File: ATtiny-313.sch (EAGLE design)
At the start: 17 parts, among them IC1 REG1117, IC2 ATtiny85

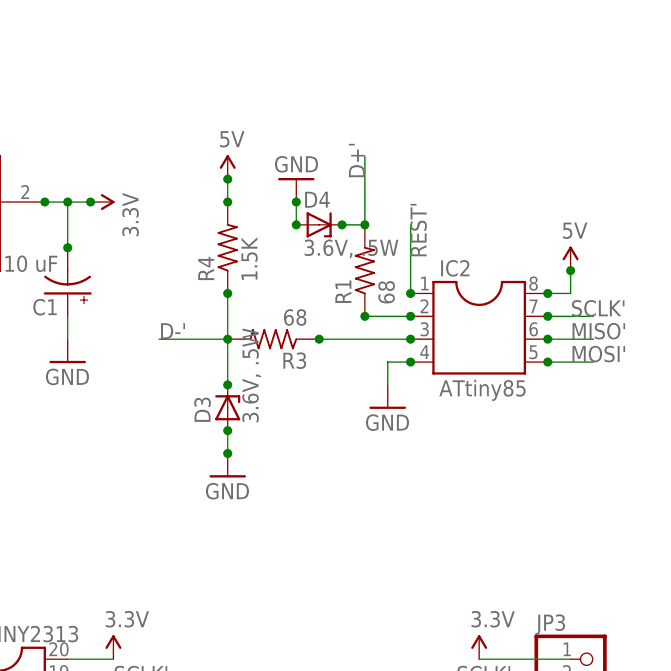
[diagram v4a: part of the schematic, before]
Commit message: run ISP off 3.3v
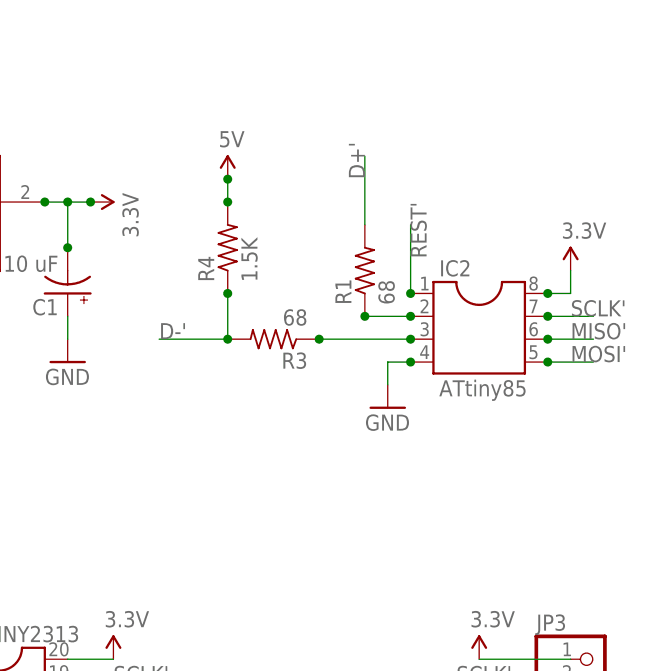
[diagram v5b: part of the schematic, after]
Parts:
- removed D3, D4: 3.6V, .5W, diode:ZENER-DIODEDO35Z10
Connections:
- net 3.3V: now also IC2.8
- net 5V: no longer IC2.8
- net D+': no longer D4.C
- net D-': no longer D3.C
- net GND: no longer D3.A, D4.A
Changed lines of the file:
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@@
 <part name="R3" library="resistor" deviceset="R-US_" device="R3216" value="68"/>
 <part name="R4" library="resistor" deviceset="R-US_" device="R3216" value="1.5K"/>
-<part name="SUPPLY8" library="SparkFun-Aesthetics" deviceset="5V" device=""/>
-<part name="GND10" library="SparkFun-Aesthetics" deviceset="GND" device=""/>
 <part name="SUPPLY9" library="SparkFun-Aesthetics" deviceset="5V" device=""/>
-<part name="GND11" library="SparkFun-Aesthetics" deviceset="GND" device=""/>
-<part name="D3" library="diode" deviceset="ZENER-DIODE" device="DO35Z10" value="3.6V, .5W"/>
-<part name="D4" library="diode" deviceset="ZENER-DIODE" device="DO35Z10" value="3.6V, .5W"/>
+<part name="SUPPLY8" library="SparkFun-Aesthetics" deviceset="3.3V" device=""/>
 </parts>
 <sheets>
@@
 <instance part="R3" gate="G$1" x="91.44" y="53.34" rot="R180"/>
 <instance part="R4" gate="G$1" x="86.36" y="63.5" rot="R90"/>
+<instance part="SUPPLY9" gate="G$1" x="86.36" y="71.12"/>
 <instance part="SUPPLY8" gate="G$1" x="124.46" y="60.96"/>
-<instance part="GND10" gate="1" x="86.36" y="38.1"/>
-<instance part="SUPPLY9" gate="G$1" x="86.36" y="71.12"/>
-<instance part="GND11" gate="1" x="93.98" y="71.12" rot="R180"/>
-<instance part="D3" gate="G$1" x="86.36" y="45.72" rot="R90"/>
-<instance part="D4" gate="G$1" x="96.52" y="66.04"/>
 </instances>
 <busses>
@@
 <junction x="71.12" y="68.58"/>
 </segment>
+<segment>
+<pinref part="IC2" gate="G$1" pin="8"/>
+<wire x1="121.92" y1="58.42" x2="124.46" y2="58.42" width="0.1524" layer="91"/>
+<wire x1="124.46" y1="58.42" x2="124.46" y2="60.96" width="0.1524" layer="91"/>
+<junction x="121.92" y="58.42"/>
+<pinref part="SUPPLY8" gate="G$1" pin="3.3V"/>
+</segment>
 </net>
 <net name="GND" class="0">
@@
 <pinref part="IC2" gate="G$1" pin="4"/>
 <junction x="106.68" y="50.8"/>
-</segment>
-<segment>
-<pinref part="GND10" gate="1" pin="GND"/>
-<wire x1="86.36" y1="40.64" x2="86.36" y2="43.18" width="0.1524" layer="91"/>
-<junction x="86.36" y="40.64"/>
-<pinref part="D3" gate="G$1" pin="A"/>
-<junction x="86.36" y="43.18"/>
-</segment>
-<segment>
-<pinref part="GND11" gate="1" pin="GND"/>
-<wire x1="93.98" y1="68.58" x2="93.98" y2="66.04" width="0.1524" layer="91"/>
-<junction x="93.98" y="68.58"/>
-<pinref part="D4" gate="G$1" pin="A"/>
-<junction x="93.98" y="66.04"/>
 </segment>
 </net>
@@
 </segment>
 <segment>
-<pinref part="IC2" gate="G$1" pin="8"/>
-<wire x1="121.92" y1="58.42" x2="124.46" y2="58.42" width="0.1524" layer="91"/>
-<pinref part="SUPPLY8" gate="G$1" pin="5V"/>
-<wire x1="124.46" y1="58.42" x2="124.46" y2="60.96" width="0.1524" layer="91"/>
-<junction x="121.92" y="58.42"/>
-<junction x="124.46" y="60.96"/>
-</segment>
-<segment>
 <pinref part="SUPPLY9" gate="G$1" pin="5V"/>
 <pinref part="R4" gate="G$1" pin="2"/>
@@
 <segment>
 <pinref part="R3" gate="G$1" pin="2"/>
-<wire x1="86.36" y1="48.26" x2="86.36" y2="53.34" width="0.1524" layer="91"/>
 <junction x="86.36" y="53.34"/>
 <wire x1="86.36" y1="53.34" x2="78.74" y2="53.34" width="0.1524" layer="91"/>
@@
 <wire x1="86.36" y1="53.34" x2="86.36" y2="58.42" width="0.1524" layer="91"/>
 <junction x="86.36" y="58.42"/>
-<pinref part="D3" gate="G$1" pin="C"/>
-<junction x="86.36" y="48.26"/>
 </segment>
 </net>
@@
 <segment>
 <pinref part="R1" gate="G$1" pin="2"/>
-<wire x1="99.06" y1="66.04" x2="101.6" y2="66.04" width="0.1524" layer="91"/>
-<junction x="101.6" y="66.04"/>
 <wire x1="101.6" y1="66.04" x2="101.6" y2="73.66" width="0.1524" layer="91"/>
-<pinref part="D4" gate="G$1" pin="C"/>
-<junction x="99.06" y="66.04"/>
-</segment>
-</net>
+</segment>
+</net>

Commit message: work on rev 3
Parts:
- removed JP1: USB-B, SparkFun-Connectors:USBPTH
- added JP5: (no value), pinhead:PINHD-1X2
- added U$1: USB-MINIB-5PIN, SparkFun-Connectors:USB-MINIB-5PIN
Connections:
- new net N$3: C1.-, IC1.VOUT, JP5.1
- net 3.3V: now also JP5.2, R4.2; no longer C1.-, IC1.VOUT
- net 5V: now also U$1.VBUS; no longer JP1.VBUS, R4.2
- net D+': no longer JP1.D+
- net D-': no longer JP1.D-
- net GND: now also U$1.GND; no longer JP1.GND
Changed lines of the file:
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@@
 <parts>
 <part name="ATTINY2313" library="ic-package" deviceset="DIL20" device="S"/>
-<part name="JP1" library="SparkFun-Connectors" deviceset="USB" device="PTH" value="USB-B"/>
 <part name="C1" library="rcl" deviceset="CPOL-US" device="E1.8-4" value="10 uF"/>
 <part name="C2" library="rcl" deviceset="CPOL-US" device="E1.8-4" value="10 uF"/>
@@
 <part name="SUPPLY3" library="SparkFun-Aesthetics" deviceset="3.3V" device=""/>
 <part name="SUPPLY4" library="SparkFun-Aesthetics" deviceset="3.3V" device=""/>
-<part name="GND1" library="SparkFun-Aesthetics" deviceset="GND" device=""/>
 <part name="GND2" library="SparkFun-Aesthetics" deviceset="GND" device=""/>
 <part name="GND3" library="SparkFun-Aesthetics" deviceset="GND" device=""/>
@@
 <part name="GND8" library="SparkFun-Aesthetics" deviceset="GND" device=""/>
 <part name="GND9" library="SparkFun-Aesthetics" deviceset="GND" device=""/>
-<part name="SUPPLY5" library="SparkFun-Aesthetics" deviceset="5V" device=""/>
 <part name="SUPPLY6" library="SparkFun-Aesthetics" deviceset="5V" device=""/>
 <part name="SUPPLY7" library="SparkFun-Aesthetics" deviceset="5V" device=""/>
@@
 <part name="R3" library="resistor" deviceset="R-US_" device="R3216" value="68"/>
 <part name="R4" library="resistor" deviceset="R-US_" device="R3216" value="1.5K"/>
-<part name="SUPPLY9" library="SparkFun-Aesthetics" deviceset="5V" device=""/>
 <part name="SUPPLY8" library="SparkFun-Aesthetics" deviceset="3.3V" device=""/>
+<part name="SUPPLY9" library="SparkFun-Aesthetics" deviceset="3.3V" device=""/>
+<part name="JP5" library="pinhead" deviceset="PINHD-1X2" device=""/>
+<part name="U$1" library="SparkFun-Connectors" deviceset="USB-MINIB" device="-5PIN"/>
+<part name="SUPPLY10" library="SparkFun-Aesthetics" deviceset="5V" device=""/>
+<part name="GND10" library="SparkFun-Aesthetics" deviceset="GND" device=""/>
 </parts>
 <sheets>
@@
 <instances>
 <instance part="ATTINY2313" gate="G$1" x="60.96" y="7.62"/>
-<instance part="JP1" gate="G$1" x="25.4" y="83.82" rot="R90"/>
 <instance part="C1" gate="G$1" x="68.58" y="58.42" rot="R180"/>
 <instance part="C2" gate="G$1" x="33.02" y="58.42" rot="R180"/>
@@
 <instance part="R2" gate="G$1" x="-7.62" y="45.72" rot="R90"/>
 <instance part="IC1" gate="G$1" x="53.34" y="68.58"/>
-<instance part="SUPPLY1" gate="G$1" x="71.12" y="68.58" rot="R270"/>
+<instance part="SUPPLY1" gate="G$1" x="76.2" y="73.66"/>
 <instance part="SUPPLY2" gate="G$1" x="-7.62" y="68.58"/>
 <instance part="SUPPLY3" gate="G$1" x="73.66" y="17.78"/>
 <instance part="SUPPLY4" gate="G$1" x="114.3" y="17.78"/>
-<instance part="GND1" gate="1" x="30.48" y="78.74"/>
 <instance part="GND2" gate="1" x="33.02" y="50.8"/>
 <instance part="GND3" gate="1" x="-20.32" y="60.96" rot="R180"/>
@@
 <instance part="GND8" gate="1" x="12.7" y="-5.08" rot="R90"/>
 <instance part="GND9" gate="1" x="-7.62" y="35.56"/>
-<instance part="SUPPLY5" gate="G$1" x="22.86" y="78.74" rot="R180"/>
 <instance part="SUPPLY6" gate="G$1" x="5.08" y="68.58"/>
 <instance part="SUPPLY7" gate="G$1" x="30.48" y="68.58" rot="R90"/>
@@
 <instance part="R3" gate="G$1" x="91.44" y="53.34" rot="R180"/>
 <instance part="R4" gate="G$1" x="86.36" y="63.5" rot="R90"/>
+<instance part="SUPPLY8" gate="G$1" x="124.46" y="60.96"/>
 <instance part="SUPPLY9" gate="G$1" x="86.36" y="71.12"/>
-<instance part="SUPPLY8" gate="G$1" x="124.46" y="60.96"/>
+<instance part="JP5" gate="G$1" x="76.2" y="71.12" rot="R90"/>
+<instance part="U$1" gate="G$1" x="15.24" y="93.98" rot="R90"/>
+<instance part="SUPPLY10" gate="G$1" x="5.08" y="86.36" rot="R180"/>
+<instance part="GND10" gate="1" x="15.24" y="83.82"/>
 </instances>
 <busses>
@@
 </segment>
 <segment>
-<pinref part="C1" gate="G$1" pin="-"/>
-<wire x1="68.58" y1="68.58" x2="68.58" y2="63.5" width="0.1524" layer="91"/>
-<junction x="68.58" y="63.5"/>
-<pinref part="IC1" gate="G$1" pin="VOUT"/>
-<wire x1="68.58" y1="68.58" x2="66.04" y2="68.58" width="0.1524" layer="91"/>
-<junction x="66.04" y="68.58"/>
-<pinref part="SUPPLY1" gate="G$1" pin="3.3V"/>
-<wire x1="68.58" y1="68.58" x2="71.12" y2="68.58" width="0.1524" layer="91"/>
-<junction x="68.58" y="68.58"/>
-<junction x="71.12" y="68.58"/>
-</segment>
-<segment>
 <pinref part="IC2" gate="G$1" pin="8"/>
 <wire x1="121.92" y1="58.42" x2="124.46" y2="58.42" width="0.1524" layer="91"/>
@@
 <pinref part="SUPPLY8" gate="G$1" pin="3.3V"/>
 </segment>
+<segment>
+<pinref part="R4" gate="G$1" pin="2"/>
+<wire x1="86.36" y1="71.12" x2="86.36" y2="68.58" width="0.1524" layer="91"/>
+<junction x="86.36" y="68.58"/>
+<pinref part="SUPPLY9" gate="G$1" pin="3.3V"/>
+</segment>
+<segment>
+<pinref part="JP5" gate="G$1" pin="2"/>
+<pinref part="SUPPLY1" gate="G$1" pin="3.3V"/>
+<wire x1="76.2" y1="68.58" x2="76.2" y2="73.66" width="0.1524" layer="91"/>
+<junction x="76.2" y="68.58"/>
+<junction x="76.2" y="73.66"/>
+</segment>
 </net>
 <net name="GND" class="0">
-<segment>
-<pinref part="JP1" gate="G$1" pin="GND"/>
-<pinref part="GND1" gate="1" pin="GND"/>
-<wire x1="25.4" y1="81.28" x2="30.48" y2="81.28" width="0.1524" layer="91"/>
-</segment>
 <segment>
 <pinref part="C2" gate="G$1" pin="+"/>
@@
 <pinref part="IC2" gate="G$1" pin="4"/>
 <junction x="106.68" y="50.8"/>
+</segment>
+<segment>
+<pinref part="U$1" gate="G$1" pin="GND"/>
+<wire x1="15.24" y1="91.44" x2="15.24" y2="86.36" width="0.1524" layer="91"/>
+<pinref part="GND10" gate="1" pin="GND"/>
 </segment>
 </net>
@@
 </segment>
 <segment>
-<pinref part="SUPPLY5" gate="G$1" pin="5V"/>
-<pinref part="JP1" gate="G$1" pin="VBUS"/>
-<wire x1="22.86" y1="78.74" x2="22.86" y2="81.28" width="0.1524" layer="91"/>
-</segment>
-<segment>
-<pinref part="SUPPLY9" gate="G$1" pin="5V"/>
-<pinref part="R4" gate="G$1" pin="2"/>
-<wire x1="86.36" y1="71.12" x2="86.36" y2="68.58" width="0.1524" layer="91"/>
-<junction x="86.36" y="71.12"/>
-<junction x="86.36" y="68.58"/>
+<pinref part="U$1" gate="G$1" pin="VBUS"/>
+<wire x1="5.08" y1="91.44" x2="5.08" y2="86.36" width="0.1524" layer="91"/>
+<pinref part="SUPPLY10" gate="G$1" pin="5V"/>
 </segment>
 </net>
@@
 <net name="D-'" class="0">
 <segment>
-<pinref part="JP1" gate="G$1" pin="D-"/>
-<wire x1="20.32" y1="81.28" x2="20.32" y2="76.2" width="0.1524" layer="91"/>
+<wire x1="7.62" y1="91.44" x2="7.62" y2="86.36" width="0.1524" layer="91"/>
 </segment>
 <segment>
@@
 <net name="D+'" class="0">
 <segment>
-<pinref part="JP1" gate="G$1" pin="D+"/>
-<wire x1="17.78" y1="81.28" x2="17.78" y2="76.2" width="0.1524" layer="91"/>
+<wire x1="10.16" y1="91.44" x2="10.16" y2="86.36" width="0.1524" layer="91"/>
 </segment>
 <segment>
@@
 </segment>
 </net>
+<net name="N$3" class="0">
+<segment>
+<pinref part="C1" gate="G$1" pin="-"/>
+<wire x1="68.58" y1="68.58" x2="68.58" y2="63.5" width="0.1524" layer="91"/>
+<junction x="68.58" y="63.5"/>
+<pinref part="IC1" gate="G$1" pin="VOUT"/>
+<wire x1="68.58" y1="68.58" x2="66.04" y2="68.58" width="0.1524" layer="91"/>
+<junction x="66.04" y="68.58"/>
+<pinref part="JP5" gate="G$1" pin="1"/>
+<wire x1="68.58" y1="68.58" x2="73.66" y2="68.58" width="0.1524" layer="91"/>
+<junction x="73.66" y="68.58"/>
+<junction x="68.58" y="68.58"/>
+</segment>
+</net>

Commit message: more SMD goodness
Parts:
- removed IC2: ATtiny85, ic-package:DIL8
- removed JP5: (no value), pinhead:PINHD-1X2
- added U1: ATTINY85-20SU, Atmel_By_element14_Batch_1:ATTINY85-20SU
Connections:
- removed net N$1: IC2.2, R1.1
- removed net N$2: IC2.3, R3.1
- removed net N$3: C1.-, IC1.VOUT, JP5.1
- new net N$15: R3.1, U1.PB4
- new net N$16: R1.1, U1.PB3
- net 3.3V: now also C1.-, IC1.VOUT, U1.VCC; no longer IC2.8, JP5.2
- net GND: now also U1.GND; no longer IC2.4
- net MISO': now also U1.PB1; no longer IC2.6
- net MOSI': now also U1.PB0; no longer IC2.5
- net REST': now also U1.PB5; no longer IC2.1
- net SCLK': now also U1.PB2; no longer IC2.7
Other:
- moved on the sheet: R1, R3, R4
